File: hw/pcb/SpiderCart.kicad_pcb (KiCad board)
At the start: 4 copper layers, 51 x 60.7 mm, 59 parts, among them J1 GameBoy_Cartridge, J2 USB_C_Receptacle_USB2.0_16P, J4 Conn_01x03, J5 Conn_01x02, J6 TF-01A, Q1 AO3401A, U1 RP2354B, U10 LIS3DH, U2 NCP1117-3.3_SOT223, U4 TXS0108EPW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

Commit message: Add I2C extension pins, and SWD pins
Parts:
- added J3: Conn_01x04, Connector_PinHeader_1.27mm:PinHeader_1x04_P1.27mm_Vertical, F.Cu at (137.0, 57.1)
- added TP3: SWCLK, TestPoint:TestPoint_Pad_D1.5mm, F.Cu at (166.9, 71.3)
- added TP4: SWDIO, TestPoint:TestPoint_Pad_D1.5mm, F.Cu at (164.4, 71.3)
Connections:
- U1 pad 33: unconnected-(U1-SWCLK-Pad33) -> Net-(U1-SWCLK)
- U1 pad 34: unconnected-(U1-SWDIO-Pad34) -> Net-(U1-SWDIO)
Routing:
- net +5V: track 91.7 -> 113.7 mm
- net Net-(U1-SWCLK): track 0.00 -> 8.53 mm
- net Net-(U1-SWDIO): track 0.00 -> 6.33 mm
- net /SDA: track 58.2 -> 63.6 mm
- net /SCL: track 65.3 -> 69.7 mm
- net /~{MEM_OE}: track 23.4 -> 26.9 mm
- net /D2: track 42.9 -> 43.8 mm
- net /D1: track 38.7 -> 39.3 mm
- net /D0: track 36.4 -> 37.1 mm

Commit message: Add V1 text
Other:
- board text added: "SpiderCart V1"
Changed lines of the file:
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@@
 			)
 		)
+		(attr exclude_from_pos_files exclude_from_bom)
 		(duplicate_pad_numbers_are_jumpers no)
 		(fp_circle
@@
 			)
 		)
+		(attr exclude_from_pos_files exclude_from_bom)
 		(duplicate_pad_numbers_are_jumpers no)
 		(fp_circle
@@
 			)
 		)
-		(attr smd)
+		(attr smd exclude_from_pos_files exclude_from_bom)
 		(duplicate_pad_numbers_are_jumpers no)
 		(fp_line
@@
 		(layer "Edge.Cuts")
 	)
+	(gr_text "SpiderCart V1"
+		(at 167.2336 58.2676 0)
+		(layer "F.SilkS")
+		(effects
+			(font
+				(size 1 1)
+				(thickness 0.15)
+			)
+			(justify left bottom)
+		)
+	)
 	(gr_text "JLCJLCJLCJLC"
 		(at 145.6944 66.9036 90)
@@
 	)
 	(segment
+		(start 165.8788 72.3224)
+		(end 166.9288 71.2724)
+		(width 0.2)
+		(layer "F.Cu")
+		(net "Net-(U1-SWCLK)")
+	)
+	(segment
+		(start 164.604365 72.3224)
+		(end 165.8788 72.3224)
+		(width 0.2)
+		(layer "F.Cu")
+		(net "Net-(U1-SWCLK)")
+	)
+	(segment
+		(start 160.0902 75.3618)
+		(end 161.564965 75.3618)
+		(width 0.2)
+		(layer "F.Cu")
+		(net "Net-(U1-SWCLK)")
+	)
+	(segment
+		(start 161.564965 75.3618)
+		(end 164.604365 72.3224)
+		(width 0.2)
+		(layer "F.Cu")
+		(net "Net-(U1-SWCLK)")
+	)
+	(segment
+		(start 160.0902 74.9618)
+		(end 161.554843 74.9618)
+		(width 0.2)
+		(layer "F.Cu")
+		(net "Net-(U1-SWDIO)")
+	)
+	(segment
+		(start 164.3888 72.127843)
+		(end 164.3888 71.2724)
+		(width 0.2)
+		(layer "F.Cu")
+		(net "Net-(U1-SWDIO)")
+	)
+	(segment
+		(start 161.554843 74.9618)
+		(end 164.3888 72.127843)
+		(width 0.2)
+		(layer "F.Cu")
+		(net "Net-(U1-SWDIO)")
+	)
+	(segment
 		(start 164.01 80.79)
 		(end 166.165 82.945)
@@
 		(net "Net-(J1-~{RES})")
 	)
-	(segment
-		(start 165.8788 72.3224)
-		(end 166.9288 71.2724)
-		(width 0.2)
-		(layer "F.Cu")
-		(net "Net-(U1-SWCLK)")
-	)
-	(segment
-		(start 164.604365 72.3224)
-		(end 165.8788 72.3224)
-		(width 0.2)
-		(layer "F.Cu")
-		(net "Net-(U1-SWCLK)")
-	)
-	(segment
-		(start 160.0902 75.3618)
-		(end 161.564965 75.3618)
-		(width 0.2)
-		(layer "F.Cu")
-		(net "Net-(U1-SWCLK)")
-	)
-	(segment
-		(start 161.564965 75.3618)
-		(end 164.604365 72.3224)
-		(width 0.2)
-		(layer "F.Cu")
-		(net "Net-(U1-SWCLK)")
-	)
-	(segment
-		(start 160.0902 74.9618)
-		(end 161.554843 74.9618)
-		(width 0.2)
-		(layer "F.Cu")
-		(net "Net-(U1-SWDIO)")
-	)
-	(segment
-		(start 164.3888 72.127843)
-		(end 164.3888 71.2724)
-		(width 0.2)
-		(layer "F.Cu")
-		(net "Net-(U1-SWDIO)")
-	)
-	(segment
-		(start 161.554843 74.9618)
-		(end 164.3888 72.127843)
-		(width 0.2)
-		(layer "F.Cu")
-		(net "Net-(U1-SWDIO)")
-	)
 	(zone

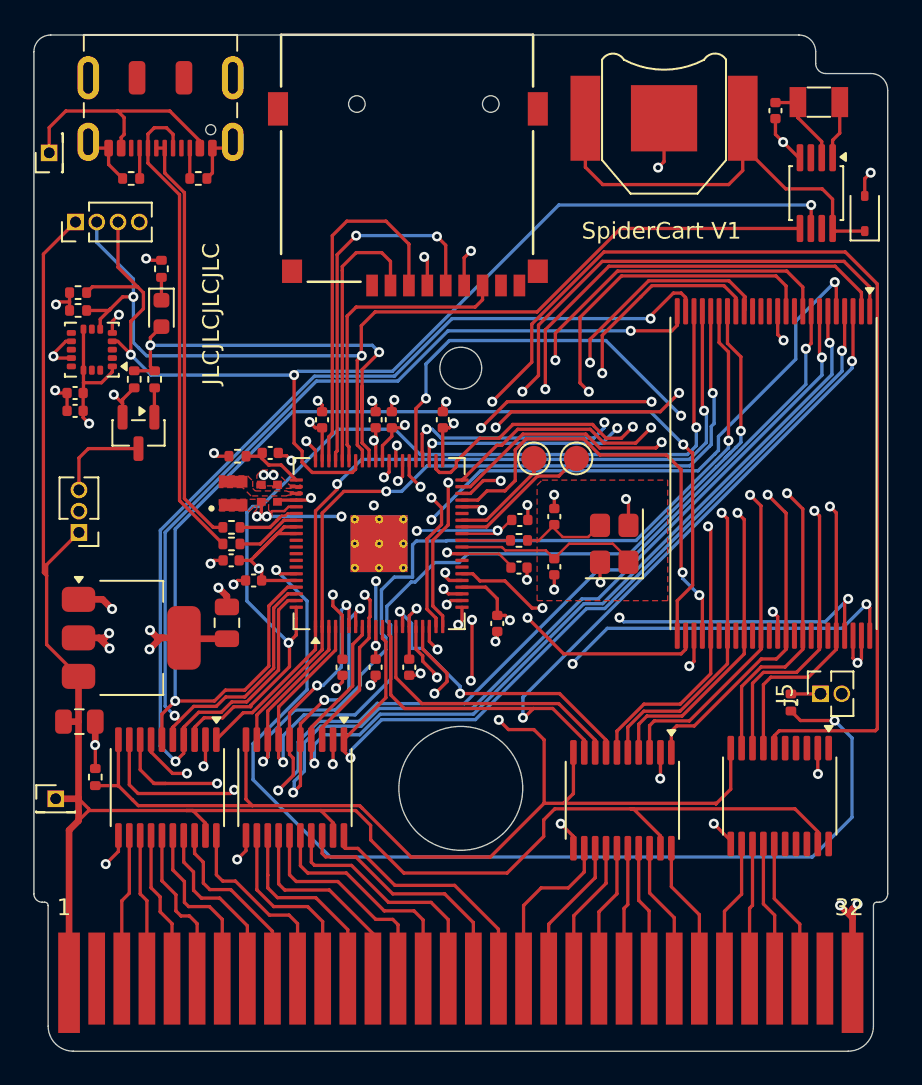
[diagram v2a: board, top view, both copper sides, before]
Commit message: Correct issues found in V1 production. I2C pullups where pulldowns, USB D- and D+ where swapped.
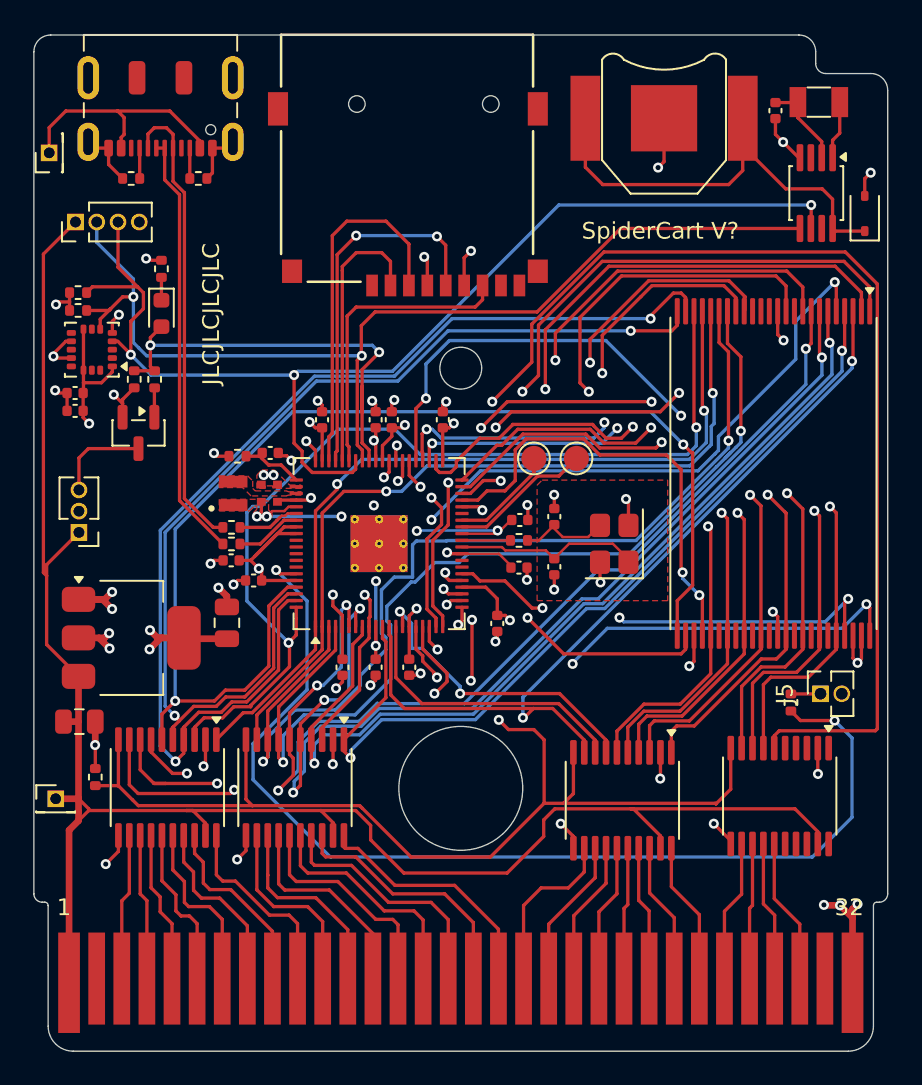
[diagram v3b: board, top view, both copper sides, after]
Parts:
- turned R13 to 0 degrees
- turned R14 to 0 degrees
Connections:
- R13 pad 1: /SDA -> +3V3
- R13 pad 2: GND -> /SDA
- R14 pad 1: /SCL -> +3V3
- R14 pad 2: GND -> /SCL
- R7 pad 1: /USB_D+ -> /USB_D-
- R8 pad 1: /USB_D- -> /USB_D+
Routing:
- net +3V3: track 70.8 -> 72.8 mm, vias 24 -> 25
- net /USB_D-: track 29.0 -> 27.7 mm
- net GND: track 64.8 -> 66.1 mm, vias 39 -> 40
- net /USB_D+: track 24.9 -> 25.6 mm
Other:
- board text added: "SpiderCart V?"
- board text removed: "SpiderCart V1"
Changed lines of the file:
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@@
 	(generator_version "10.0")
 	(general
-		(thickness 1.6)
+		(thickness 0.8)
 		(legacy_teardrops no)
 	)
 	(paper "A4")
 	(layers
-		(0 "F.Cu" jumper)
+		(0 "F.Cu" signal)
 		(4 "In1.Cu" signal)
 		(6 "In2.Cu" signal)
@@
 			(layer "dielectric 2"
 				(type "core")
-				(thickness 1.24)
+				(thickness 0.44)
 				(material "FR4")
 				(epsilon_r 4.5)
@@
 		(capping no)
 		(filling no)
+		(zone_defaults)
 		(pcbplotparams
 			(layerselection 0x00000000_00000000_55555555_5755f5ff)
@@
 	(footprint "Resistor_SMD:R_0402_1005Metric"
 		(layer "F.Cu")
-		(at 137.16 61.3664 180)
+		(at 137.16 61.3664)
 		(descr "Resistor SMD 0402 (1005 Metric), square (rectangular) end terminal, IPC-7351 nominal, (Body size source: IPC-SM-782 page 72, https://www.pcb-3d.com/wordpress/wp-content/uploads/ipc-sm-782a_amendment_1_and_2.pdf)")
 		(tags "resistor")
@@
 		(duplicate_pad_numbers_are_jumpers no)
 		(fp_line
-			(start -0.153641 0.38)
-			(end 0.153641 0.38)
+			(start -0.153641 -0.38)
+			(end 0.153641 -0.38)
 			(stroke
 				(width 0.12)
@@
 		)
 		(fp_line
-			(start -0.153641 -0.38)
-			(end 0.153641 -0.38)
+			(start -0.153641 0.38)
+			(end 0.153641 0.38)
 			(stroke
 				(width 0.12)
@@
 		)
 		(pad "1" smd roundrect
-			(at -0.51 0 180)
+			(at -0.51 0)
 			(size 0.54 0.64)
 			(layers "F.Cu" "F.Mask" "F.Paste")
 			(roundrect_rratio 0.25)
-			(net "/SCL")
+			(net "+3V3")
 			(pintype "passive")
 		)
 		(pad "2" smd roundrect
-			(at 0.51 0 180)
+			(at 0.51 0)
 			(size 0.54 0.64)
 			(layers "F.Cu" "F.Mask" "F.Paste")
 			(roundrect_rratio 0.25)
-			(net "GND")
+			(net "/SCL")
 			(pintype "passive")
 		)
@@
 			(layers "F.Cu" "F.Mask" "F.Paste")
 			(roundrect_rratio 0.25)
-			(net "/USB_D+")
+			(net "/USB_D-")
 			(pintype "passive")
 		)
@@
 	(footprint "Resistor_SMD:R_0402_1005Metric"
 		(layer "F.Cu")
-		(at 137.16 62.4332 180)
+		(at 137.16 62.4332)
 		(descr "Resistor SMD 0402 (1005 Metric), square (rectangular) end terminal, IPC-7351 nominal, (Body size source: IPC-SM-782 page 72, https://www.pcb-3d.com/wordpress/wp-content/uploads/ipc-sm-782a_amendment_1_and_2.pdf)")
 		(tags "resistor")
@@
 		(duplicate_pad_numbers_are_jumpers no)
 		(fp_line
-			(start -0.153641 0.38)
-			(end 0.153641 0.38)
+			(start -0.153641 -0.38)
+			(end 0.153641 -0.38)
 			(stroke
 				(width 0.12)
@@
 		)
 		(fp_line
-			(start -0.153641 -0.38)
-			(end 0.153641 -0.38)
+			(start -0.153641 0.38)
+			(end 0.153641 0.38)
 			(stroke
 				(width 0.12)
@@
 		)
 		(pad "1" smd roundrect
-			(at -0.51 0 180)
+			(at -0.51 0)
 			(size 0.54 0.64)
 			(layers "F.Cu" "F.Mask" "F.Paste")
 			(roundrect_rratio 0.25)
-			(net "/SDA")
+			(net "+3V3")
 			(pintype "passive")
 		)
 		(pad "2" smd roundrect
-			(at 0.51 0 180)
+			(at 0.51 0)
 			(size 0.54 0.64)
 			(layers "F.Cu" "F.Mask" "F.Paste")
 			(roundrect_rratio 0.25)
-			(net "GND")
+			(net "/SDA")
 			(pintype "passive")
 		)
@@
 			)
 		)
-		(attr exclude_from_pos_files exclude_from_bom)
 		(duplicate_pad_numbers_are_jumpers no)
 		(fp_circle
@@
 			)
 		)
-		(attr exclude_from_pos_files exclude_from_bom)
 		(duplicate_pad_numbers_are_jumpers no)
 		(fp_circle
@@
 			(layers "F.Cu" "F.Mask" "F.Paste")
 			(roundrect_rratio 0.25)
-			(net "/USB_D-")
+			(net "/USB_D+")
 			(pintype "passive")
 		)
@@
 			)
 		)
-		(attr smd exclude_from_pos_files exclude_from_bom)
+		(attr smd)
 		(duplicate_pad_numbers_are_jumpers no)
 		(fp_line
@@
 		(layer "Edge.Cuts")
 	)
-	(gr_text "SpiderCart V1"
+	(gr_text "SpiderCart V?"
 		(at 167.2336 58.2676 0)
 		(layer "F.SilkS")
@@
 	)
 	(segment
+		(start 181.737 97.9678)
+		(end 181.7116 97.9424)
+		(width 0.4)
+		(layer "F.Cu")
+		(net "GND")
+	)
+	(segment
 		(start 155.899279 67.926421)
 		(end 156.0463 67.7794)
@@
 	)
 	(segment
-		(start 136.65 61.9252)
-		(end 136.65 62.4332)
-		(width 0.2)
-		(layer "F.Cu")
-		(net "GND")
-	)
-	(segment
 		(start 154.934079 68.4814)
 		(end 154.934079 68.038779)
@@
 	)
 	(segment
-		(start 135.9916 61.9252)
-		(end 135.8392 62.0776)
-		(width 0.2)
-		(layer "F.Cu")
-		(net "GND")
-	)
-	(segment
 		(start 178.816 51.9176)
 		(end 179.2732 52.3748)
@@
 	)
 	(segment
-		(start 139.2058 63.7758)
-		(end 139.2058 63.0798)
-		(width 0.2)
+		(start 137.185 79.6912)
+		(end 138.7488 79.6912)
+		(width 0.4)
 		(layer "F.Cu")
 		(net "GND")
 	)
 	(segment
-		(start 136.65 61.9252)
-		(end 135.9916 61.9252)
+		(start 139.2058 63.7758)
+		(end 139.2058 63.0798)
 		(width 0.2)
 		(layer "F.Cu")
@@
 	)
 	(segment
+		(start 182.6768 97.9678)
+		(end 181.737 97.9678)
+		(width 0.4)
+		(layer "F.Cu")
+		(net "GND")
+	)
+	(segment
 		(start 154.934079 84.2242)
 		(end 154.934079 84.512621)
@@
 	)
 	(segment
-		(start 136.65 61.3664)
-		(end 136.65 61.9252)
-		(width 0.2)
-		(layer "F.Cu")
-		(net "GND")
-	)
-	(segment
 		(start 136.430368 64.2758)
 		(end 135.6868 65.019368)
@@
 	)
 	(segment
+		(start 138.7488 79.6912)
+		(end 139.192 79.248)
+		(width 0.4)
+		(layer "F.Cu")
+		(net "GND")
+	)
+	(segment
 		(start 152.952879 84.619593)
 		(end 152.568236 85.004236)
@@
 	)
 	(via
+		(at 181.7116 97.9424)
+		(size 0.6)
+		(drill 0.3)
+		(layers "F.Cu" "B.Cu")
+		(net "GND")
+	)
+	(via
 		(at 159.1451 67.881)
 		(size 0.6)
@@
 	)
 	(via
+		(at 139.192 79.248)
+		(size 0.6)
+		(drill 0.3)
+		(layers "F.Cu" "B.Cu")
+		(net "GND")
+	)
+	(via
 		(at 135.7884 67.2084)
 		(size 0.6)
@@
 	)
 	(via
-		(at 135.8392 62.0776)
-		(size 0.6)
-		(drill 0.3)
-		(layers "F.Cu" "B.Cu")
-		(net "GND")
-	)
-	(via
 		(at 160.6296 58.8772)
 		(size 0.6)
@@
 	)
 	(segment
+		(start 136.65 61.9252)
+		(end 136.65 62.4332)
+		(width 0.2)
+		(layer "F.Cu")
+		(net "+3V3")
+	)
+	(segment
 		(start 142.24 81.9912)
 		(end 141.9098 81.9912)
@@
 	)
 	(segment
+		(start 135.9916 61.9252)
+		(end 135.8392 62.0776)
+		(width 0.2)
+		(layer "F.Cu")
+		(net "+3V3")
+	)
+	(segment
 		(start 156.5179 69.4414)
 		(end 156.6813 69.278)
@@
 	)
 	(segment
+		(start 136.65 61.9252)
+		(end 135.9916 61.9252)
+		(width 0.2)
+		(layer "F.Cu")
+		(net "+3V3")
+	)
+	(segment
 		(start 144.769 88.0695)
 		(end 144.769 89.546)
@@
 	)
 	(segment
+		(start 136.65 61.3664)
+		(end 136.65 61.9252)
+		(width 0.2)
+		(layer "F.Cu")
+		(net "+3V3")
+	)
+	(segment
 		(start 158.947279 69.4414)
 		(end 159.3373 69.4414)
@@
 	)
 	(via
+		(at 135.8392 62.0776)
+		(size 0.6)
+		(drill 0.3)
+		(layers "F.Cu" "B.Cu")
+		(net "+3V3")
+	)
+	(via
 		(at 181.356 90.1192)
 		(size 0.6)
@@
 	)
 	(segment
-		(start 143.51 55.4)
-		(end 142.3326 54.2226)
+		(start 143.22 55.520122)
+		(end 142.3326 54.632722)
 		(width 0.2)
 		(layer "F.Cu")
@@
 	)
 	(segment
-		(start 143.51 73.669878)
-		(end 143.51 55.4)
+		(start 142.3326 54.632722)
+		(end 142.3326 52.7352)
 		(width 0.2)
 		(layer "F.Cu")
@@
 	)
 	(segment
-		(start 145.230122 75.39)
-		(end 143.51 73.669878)
+		(start 143.22 73.79)
+		(end 143.22 55.520122)
 		(width 0.2)
 		(layer "F.Cu")
@@
 	)
 	(segment
-		(start 142.3326 54.2226)
-		(end 142.3326 52.7352)
+		(start 145.81 76.38)
+		(end 143.22 73.79)
 		(width 0.2)
 		(layer "F.Cu")
@@
 	)
 	(segment
-		(start 145.81 75.39)
-		(end 145.230122 75.39)
+		(start 142.8326 54.7226)
+		(end 142.8326 52.7352)
 		(width 0.2)
 		(layer "F.Cu")
-		(net "/USB_D+")
+		(net "/USB_D-")
 	)
 	(segment
@@
 	)
 	(segment
-		(start 143.22 73.79)
-		(end 143.22 55.520122)
+		(start 143.51 73.669878)
+		(end 143.51 55.4)
 		(width 0.2)
 		(layer "F.Cu")
@@
 	)
 	(segment
-		(start 143.22 55.520122)
-		(end 141.3326 53.632722)
+		(start 143.51 55.4)
+		(end 142.8326 54.7226)
 		(width 0.2)
 		(layer "F.Cu")
@@
 	)
 	(segment
-		(start 141.71 51.52)
-		(end 142.44 51.52)
+		(start 145.230122 75.39)
+		(end 143.51 73.669878)
 		(width 0.2)
 		(layer "F.Cu")
@@
 	)
 	(segment
-		(start 141.3326 51.8974)
-		(end 141.71 51.52)
+		(start 141.71 51.52)
+		(end 142.44 51.52)
 		(width 0.2)
 		(layer "F.Cu")
@@
 	)
 	(segment
-		(start 141.3326 53.632722)
-		(end 141.3326 52.7352)
+		(start 141.3326 51.8974)
+		(end 141.71 51.52)
 		(width 0.2)
 		(layer "F.Cu")
@@
 	)
 	(segment
-		(start 145.81 76.38)
-		(end 143.22 73.79)
+		(start 145.81 75.39)
+		(end 145.230122 75.39)
 		(width 0.2)
 		(layer "F.Cu")

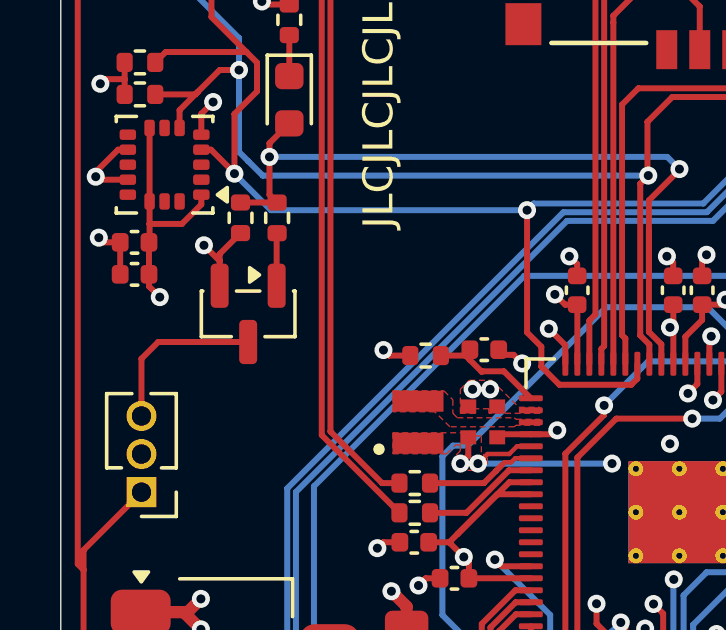
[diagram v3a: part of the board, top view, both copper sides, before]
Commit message: Fix the wrong FET in V1 design
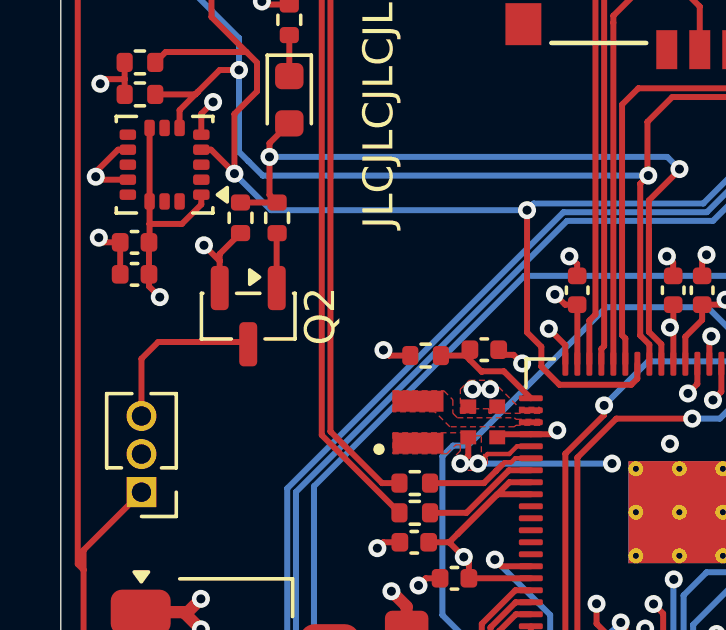
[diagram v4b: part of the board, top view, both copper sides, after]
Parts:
- removed Q1: AO3401A, Package_TO_SOT_SMD:SOT-23
- added Q2: AO3400A, Package_TO_SOT_SMD:SOT-23, F.Cu at (140.8, 69.8)
